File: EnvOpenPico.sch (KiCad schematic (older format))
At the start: 37 parts, among them J2 B3U-1000P, J3 2.54mm header 01x20, J4 2.54mm header 01x20, J5 Conn_01x03_Male, U1 SPX3819M5-L-3-3, U3 RP2040, X1 XO 32 12Mhz 3225 seiko

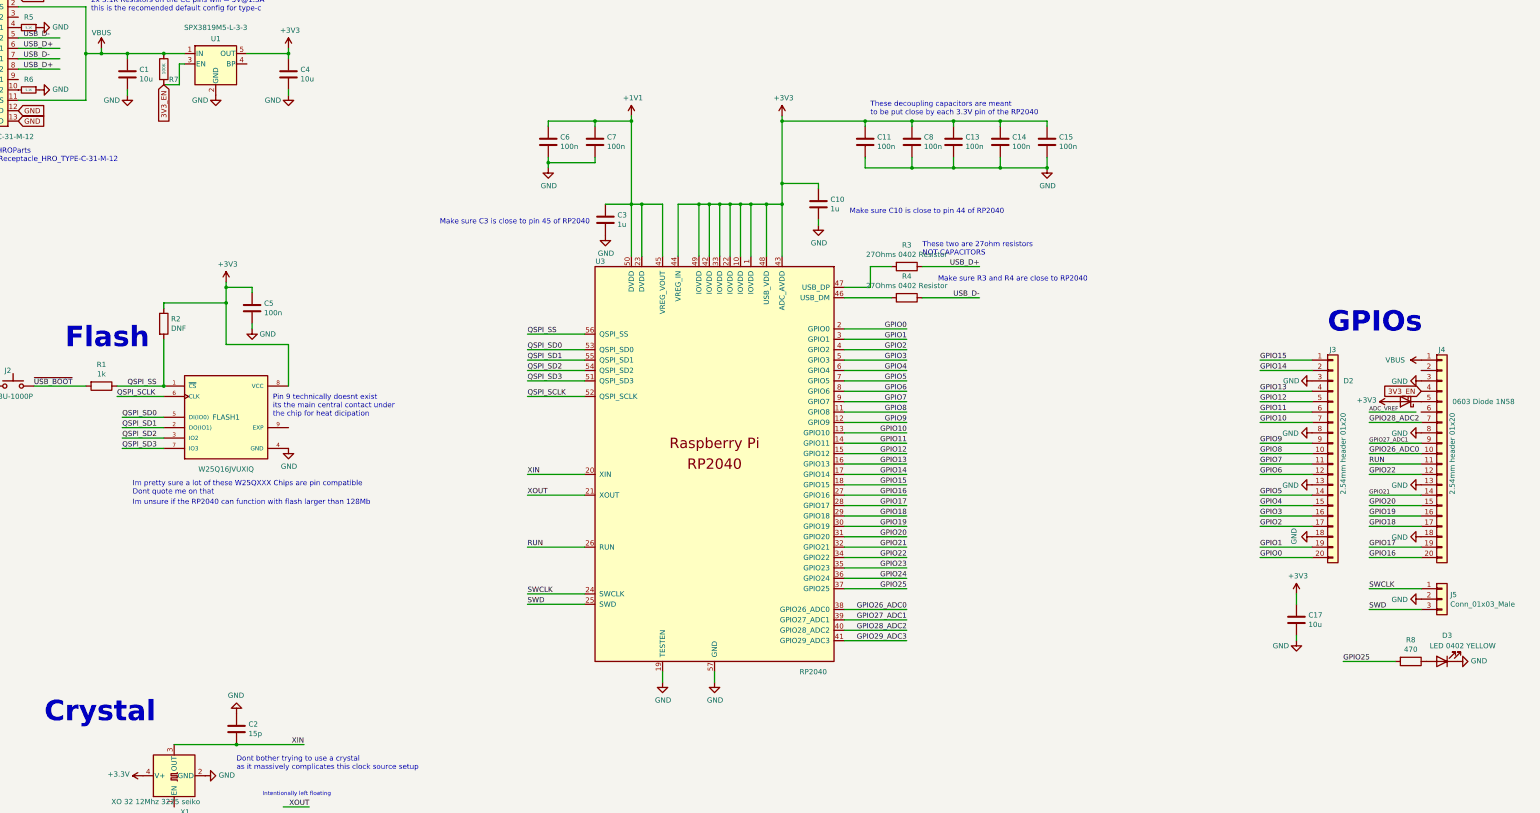
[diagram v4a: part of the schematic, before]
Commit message: Generated updated Gerber files with castelations
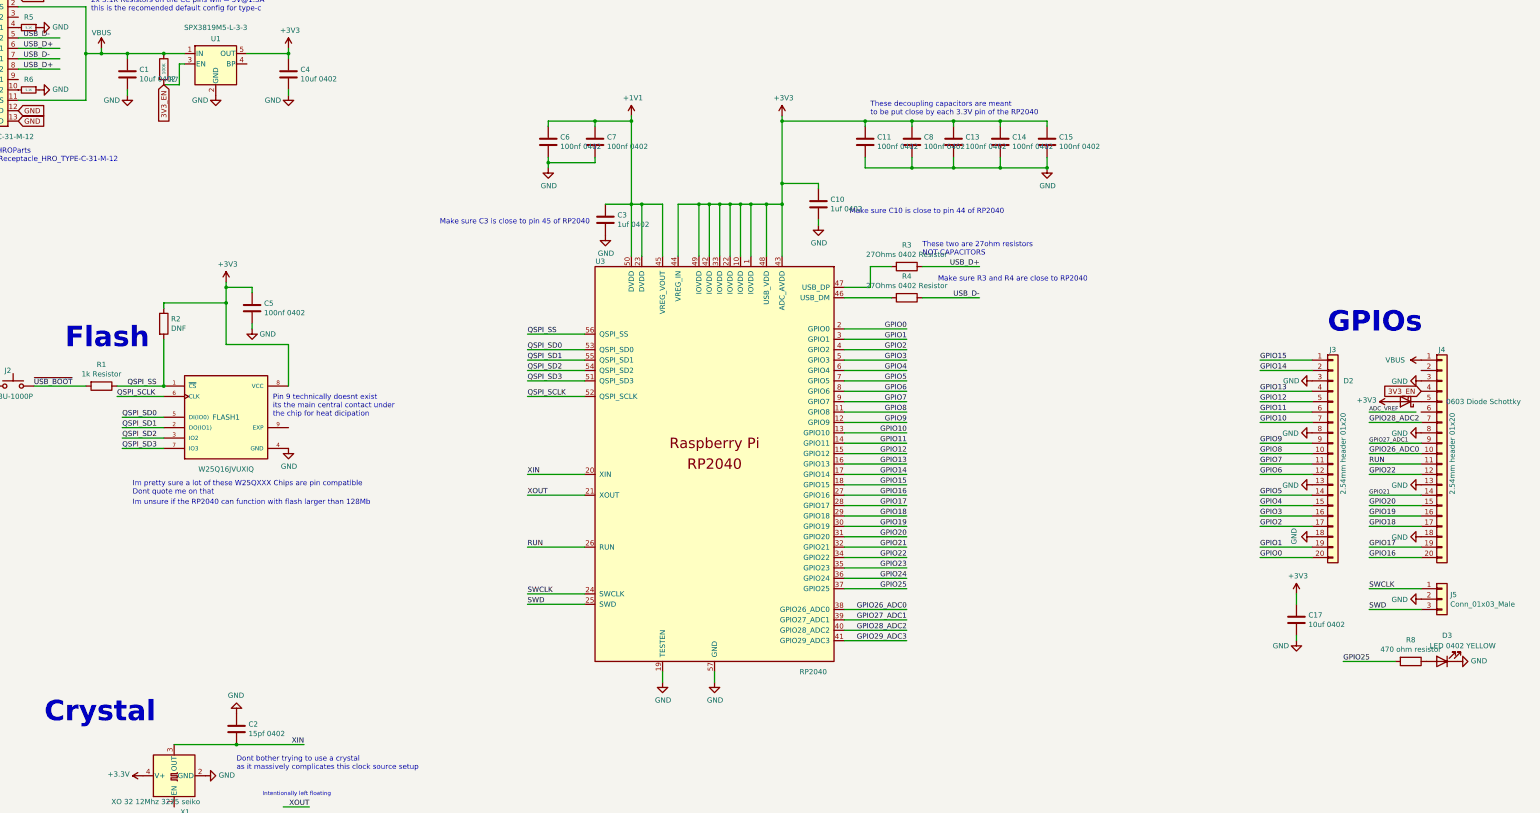
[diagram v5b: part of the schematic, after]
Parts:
- C1, C17, C4: value 10u -> 10uf 0402
- C10, C3: value 1u -> 1uf 0402
- C11, C13, C14, C15, C5, C6, C7, C8: value 100n -> 100nf 0402
- C2: value 15p -> 15pf 0402
- D2: value 0603 Diode 1N58 -> 0603 Diode Schottky
- R1: value 1k -> 1k Resistor
- R8: value 470 -> 470 ohm resistor
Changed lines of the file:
@@
 F 1 "TYPE-C-31-M-12" H 1250 950 50  0000 R CNN
 F 2 "HRO-TYPE-C31-M-12:HRO-TYPE-C-31-M-12" H 1150 1700 50  0001 C CNN
-F 3 "~" H 1150 1700 50  0001 C CNN
+F 3 "" H 1150 1700 50  0001 C CNN
 	1    1000 1750
 	1    0    0    -1
@@
 F 1 " 27Ohms 0402 Resistor" V 9534 4100 50  0000 C CNN
 F 2 "Capacitor_SMD:C_0402_1005Metric" V 9580 4100 50  0001 C CNN
-F 3 "~" H 9650 4100 50  0001 C CNN
+F 3 "" H 9650 4100 50  0001 C CNN
 	1    9650 4100
 	0    1    1    0
@@
 P 6200 2600
 F 0 "C6" H 6315 2646 50  0000 L CNN
-F 1 "100n" H 6315 2555 50  0000 L CNN
+F 1 "100nf 0402" H 6315 2555 50  0000 L CNN
 F 2 "Capacitor_SMD:C_0402_1005Metric" H 6238 2450 50  0001 C CNN
-F 3 "~" H 6200 2600 50  0001 C CNN
+F 3 "" H 6200 2600 50  0001 C CNN
 	1    6200 2600
 	1    0    0    -1
@@
 P 6650 2600
 F 0 "C7" H 6765 2646 50  0000 L CNN
-F 1 "100n" H 6765 2555 50  0000 L CNN
+F 1 "100nf 0402" H 6765 2555 50  0000 L CNN
 F 2 "Capacitor_SMD:C_0402_1005Metric" H 6688 2450 50  0001 C CNN
-F 3 "~" H 6650 2600 50  0001 C CNN
+F 3 "" H 6650 2600 50  0001 C CNN
 	1    6650 2600
 	1    0    0    -1
@@
 P 8800 3200
 F 0 "C10" H 8915 3246 50  0000 L CNN
-F 1 "1u" H 8915 3155 50  0000 L CNN
+F 1 "1uf 0402" H 8915 3155 50  0000 L CNN
 F 2 "Capacitor_SMD:C_0402_1005Metric" H 8838 3050 50  0001 C CNN
-F 3 "~" H 8800 3200 50  0001 C CNN
+F 3 "" H 8800 3200 50  0001 C CNN
 	1    8800 3200
 	1    0    0    -1
@@
 P 3350 4200
 F 0 "C5" H 3465 4246 50  0000 L CNN
-F 1 "100n" H 3465 4155 50  0000 L CNN
+F 1 "100nf 0402" H 3465 4155 50  0000 L CNN
 F 2 "Capacitor_SMD:C_0402_1005Metric" H 3388 4050 50  0001 C CNN
-F 3 "~" H 3350 4200 50  0001 C CNN
+F 3 "" H 3350 4200 50  0001 C CNN
 	1    3350 4200
 	1    0    0    -1
@@
 P 1900 4950
 F 0 "R1" V 1693 4950 50  0000 C CNN
-F 1 "1k" V 1784 4950 50  0000 C CNN
+F 1 "1k Resistor" V 1784 4950 50  0000 C CNN
 F 2 "Capacitor_SMD:C_0402_1005Metric" V 1830 4950 50  0001 C CNN
-F 3 "~" H 1900 4950 50  0001 C CNN
+F 3 "" H 1900 4950 50  0001 C CNN
 	1    1900 4950
 	0    1    1    0
@@
 F 1 "DNF" H 2570 4305 50  0000 L CNN
 F 2 "Capacitor_SMD:C_0402_1005Metric" V 2430 4350 50  0001 C CNN
-F 3 "~" H 2500 4350 50  0001 C CNN
+F 3 "" H 2500 4350 50  0001 C CNN
 	1    2500 4350
 	1    0    0    -1
@@
 F 1 "SPX3819M5-L-3-3" H 3000 2200 50  0000 C CNN
 F 2 "Package_TO_SOT_SMD:SOT-23-5" H 3000 2050 50  0001 C CNN
-F 3 "~" H 3100 1600 50  0001 C CNN
+F 3 "" H 3100 1600 50  0001 C CNN
 	1    3000 1850
 	1    0    0    -1
@@
 P 2150 1950
 F 0 "C1" H 2265 1996 50  0000 L CNN
-F 1 "10u" H 2265 1905 50  0000 L CNN
+F 1 "10uf 0402" H 2265 1905 50  0000 L CNN
 F 2 "Capacitor_SMD:C_0402_1005Metric" H 2188 1800 50  0001 C CNN
-F 3 "~" H 2150 1950 50  0001 C CNN
+F 3 "" H 2150 1950 50  0001 C CNN
 	1    2150 1950
 	1    0    0    -1
@@
 P 3700 1950
 F 0 "C4" H 3815 1996 50  0000 L CNN
-F 1 "10u" H 3815 1905 50  0000 L CNN
+F 1 "10uf 0402" H 3815 1905 50  0000 L CNN
 F 2 "Capacitor_SMD:C_0402_1005Metric" H 3738 1800 50  0001 C CNN
-F 3 "~" H 3700 1950 50  0001 C CNN
+F 3 "" H 3700 1950 50  0001 C CNN
 	1    3700 1950
 	1    0    0    -1
@@
 F 1 "B3U-1000P" H 1050 4850 50  0000 C CNN
 F 2 "Button_Switch_SMD:SW_SPST_B3U-1000P" H 1050 4950 50  0001 C CNN
-F 3 "~" H 1050 4950 50  0001 C CNN
+F 3 "" H 1050 4950 50  0001 C CNN
 	1    1050 4950
 	-1   0    0    -1
@@
 F 1 " 27Ohms  0402 Resistor" V 9534 3800 50  0000 C CNN
 F 2 "Capacitor_SMD:C_0402_1005Metric" V 9580 3800 50  0001 C CNN
-F 3 "~" H 9650 3800 50  0001 C CNN
+F 3 "" H 9650 3800 50  0001 C CNN
 	1    9650 3800
 	0    1    1    0
@@
 F 1 "2.54mm header 01x20" V 14900 5600 50  0000 C CNN
 F 2 "Connector_PinHeader_2.54mm:PinHeader_1x20_P2.54mm_Vertical" H 14800 5600 50  0001 C CNN
-F 3 "~" H 14800 5600 50  0001 C CNN
+F 3 "" H 14800 5600 50  0001 C CNN
 	1    14800 5600
 	1    0    0    -1
@@
 F 1 "2.54mm header 01x20" V 13850 5600 50  0000 C CNN
 F 2 "Connector_PinHeader_2.54mm:PinHeader_1x20_P2.54mm_Vertical" H 13750 5600 50  0001 C CNN
-F 3 "~" H 13750 5600 50  0001 C CNN
+F 3 "" H 13750 5600 50  0001 C CNN
 	1    13750 5600
 	1    0    0    -1
@@
 F 1 "MountingHole" H 10000 10155 50  0000 L CNN
 F 2 "MountingHole:MountingHole_2.2mm_M2" H 9900 10200 50  0001 C CNN
-F 3 "~" H 9900 10200 50  0001 C CNN
+F 3 "" H 9900 10200 50  0001 C CNN
 	1    9900 10200
 	1    0    0    -1
@@
 F 1 "MountingHole" H 10000 10355 50  0000 L CNN
 F 2 "MountingHole:MountingHole_2.2mm_M2" H 9900 10400 50  0001 C CNN
-F 3 "~" H 9900 10400 50  0001 C CNN
+F 3 "" H 9900 10400 50  0001 C CNN
 	1    9900 10400
 	1    0    0    -1
@@
 F 1 "MountingHole" H 10000 10555 50  0000 L CNN
 F 2 "MountingHole:MountingHole_2.2mm_M2" H 9900 10600 50  0001 C CNN
-F 3 "~" H 9900 10600 50  0001 C CNN
+F 3 "" H 9900 10600 50  0001 C CNN
 	1    9900 10600
 	1    0    0    -1
@@
 F 1 "MountingHole" H 10000 10755 50  0000 L CNN
 F 2 "MountingHole:MountingHole_2.2mm_M2" H 9900 10800 50  0001 C CNN
-F 3 "~" H 9900 10800 50  0001 C CNN
+F 3 "" H 9900 10800 50  0001 C CNN
 	1    9900 10800
 	1    0    0    -1
@@
 P 13400 7200
 F 0 "C17" H 13515 7246 50  0000 L CNN
-F 1 "10u" H 13515 7155 50  0000 L CNN
+F 1 "10uf 0402" H 13515 7155 50  0000 L CNN
 F 2 "Capacitor_SMD:C_0402_1005Metric" H 13438 7050 50  0001 C CNN
-F 3 "~" H 13400 7200 50  0001 C CNN
+F 3 "" H 13400 7200 50  0001 C CNN
 	1    13400 7200
 	1    0    0    -1
@@
 P 14450 5100
 F 0 "D2" H 15000 4900 50  0000 C CNN
-F 1 "0603 Diode 1N58" H 13700 5100 50  0000 C CNN
+F 1 "0603 Diode Schottky" H 13700 5100 50  0000 C CNN
 F 2 "Diode_SMD:D_0603_1608Metric" H 14450 5100 50  0001 C CNN
-F 3 "~" H 14450 5100 50  0001 C CNN
+F 3 "" H 14450 5100 50  0001 C CNN
 	1    14450 5100
 	-1   0    0    1
@@
 P 14500 7600
 F 0 "R8" V 14293 7600 50  0000 C CNN
-F 1 "470" V 14384 7600 50  0000 C CNN
+F 1 "470 ohm resistor" V 14384 7600 50  0000 C CNN
 F 2 "Resistor_SMD:R_0402_1005Metric" V 14430 7600 50  0001 C CNN
-F 3 "~" H 14500 7600 50  0001 C CNN
+F 3 "" H 14500 7600 50  0001 C CNN
 	1    14500 7600
 	0    1    1    0
@@
 F 1 "LED 0402 YELLOW" H 14600 7450 50  0000 C CNN
 F 2 "LED_SMD:LED_0402_1005Metric" H 14800 7600 50  0001 C CNN
-F 3 "~" H 14800 7600 50  0001 C CNN
+F 3 "" H 14800 7600 50  0001 C CNN
 	1    14800 7600
 	-1   0    0    1
@@
 F 1 "Conn_01x03_Male" H 14880 6951 50  0000 L CNN
 F 2 "Connector_PinHeader_2.54mm:PinHeader_1x03_P2.54mm_Vertical" H 14800 7000 50  0001 C CNN
-F 3 "~" H 14800 7000 50  0001 C CNN
+F 3 "" H 14800 7000 50  0001 C CNN
 	1    14800 7000
 	1    0    0    -1
@@
 P 9250 2600
 F 0 "C11" H 9365 2646 50  0000 L CNN
-F 1 "100n" H 9365 2555 50  0000 L CNN
+F 1 "100nf 0402" H 9365 2555 50  0000 L CNN
 F 2 "Capacitor_SMD:C_0402_1005Metric" H 9288 2450 50  0001 C CNN
-F 3 "~" H 9250 2600 50  0001 C CNN
+F 3 "" H 9250 2600 50  0001 C CNN
 	1    9250 2600
 	1    0    0    -1
@@
 P 11000 2600
 F 0 "C15" H 11115 2646 50  0000 L CNN
-F 1 "100n" H 11115 2555 50  0000 L CNN
+F 1 "100nf 0402" H 11115 2555 50  0000 L CNN
 F 2 "Capacitor_SMD:C_0402_1005Metric" H 11038 2450 50  0001 C CNN
-F 3 "~" H 11000 2600 50  0001 C CNN
+F 3 "" H 11000 2600 50  0001 C CNN
 	1    11000 2600
 	1    0    0    -1
@@
 P 10550 2600
 F 0 "C14" H 10665 2646 50  0000 L CNN
-F 1 "100n" H 10665 2555 50  0000 L CNN
+F 1 "100nf 0402" H 10665 2555 50  0000 L CNN
 F 2 "Capacitor_SMD:C_0402_1005Metric" H 10588 2450 50  0001 C CNN
-F 3 "~" H 10550 2600 50  0001 C CNN
+F 3 "" H 10550 2600 50  0001 C CNN
 	1    10550 2600
 	1    0    0    -1
@@
 P 10100 2600
 F 0 "C13" H 10215 2646 50  0000 L CNN
-F 1 "100n" H 10215 2555 50  0000 L CNN
+F 1 "100nf 0402" H 10215 2555 50  0000 L CNN
 F 2 "Capacitor_SMD:C_0402_1005Metric" H 10138 2450 50  0001 C CNN
-F 3 "~" H 10100 2600 50  0001 C CNN
+F 3 "" H 10100 2600 50  0001 C CNN
 	1    10100 2600
 	1    0    0    -1
@@
 F 1 "XO 32 12Mhz 3225 seiko" V 2350 8450 50  0000 L CNN
 F 2 "Crystal:Crystal_SMD_SeikoEpson_TSX3225-4Pin_3.2x2.5mm" H 3300 8350 50  0001 C CNN
-F 3 "http://cdn-reichelt.de/documents/datenblatt/B400/XO32.pdf" H 2500 8700 50  0001 C CNN
+F 3 "" H 2500 8700 50  0001 C CNN
 	1    2600 8700
 	0    -1   -1   0
@@
 P 3200 8250
 F 0 "C2" H 3315 8296 50  0000 L CNN
-F 1 "15p" H 3315 8205 50  0000 L CNN
+F 1 "15pf 0402" H 3315 8205 50  0000 L CNN
 F 2 "Capacitor_SMD:C_0402_1005Metric" H 3238 8100 50  0001 C CNN
-F 3 "~" H 3200 8250 50  0001 C CNN
+F 3 "" H 3200 8250 50  0001 C CNN
 	1    3200 8250
 	1    0    0    -1
@@
 P 6750 3350
 F 0 "C3" H 6865 3396 50  0000 L CNN
-F 1 "1u" H 6865 3305 50  0000 L CNN
+F 1 "1uf 0402" H 6865 3305 50  0000 L CNN
 F 2 "Capacitor_SMD:C_0402_1005Metric" H 6788 3200 50  0001 C CNN
-F 3 "~" H 6750 3350 50  0001 C CNN
+F 3 "" H 6750 3350 50  0001 C CNN
 	1    6750 3350
 	1    0    0    -1
@@
 P 9700 2600
 F 0 "C8" H 9815 2646 50  0000 L CNN
-F 1 "100n" H 9815 2555 50  0000 L CNN
+F 1 "100nf 0402" H 9815 2555 50  0000 L CNN
 F 2 "Capacitor_SMD:C_0402_1005Metric" H 9738 2450 50  0001 C CNN
-F 3 "~" H 9700 2600 50  0001 C CNN
+F 3 "" H 9700 2600 50  0001 C CNN
 	1    9700 2600
 	1    0    0    -1
@@
 F 1 "5.1K" V 1200 2100 20  0000 C CNN
 F 2 "Resistor_SMD:R_0402_1005Metric" H 1200 2100 50  0001 C CNN
-F 3 "~" H 1200 2100 50  0001 C CNN
+F 3 "" H 1200 2100 50  0001 C CNN
 	1    1200 2100
 	0    1    1    0
@@
 F 1 "5.1K" V 1200 1500 20  0000 C CNN
 F 2 "Resistor_SMD:R_0402_1005Metric" H 1200 1500 50  0001 C CNN
-F 3 "~" H 1200 1500 50  0001 C CNN
+F 3 "" H 1200 1500 50  0001 C CNN
 	1    1200 1500
 	0    1    1    0
@@
 F 1 "100K" V 2500 1850 30  0000 L CNN
 F 2 "Resistor_SMD:R_0402_1005Metric" V 2430 1900 50  0001 C CNN
-F 3 "~" H 2500 1900 50  0001 C CNN
+F 3 "" H 2500 1900 50  0001 C CNN
 	1    2500 1900
 	1    0    0    -1

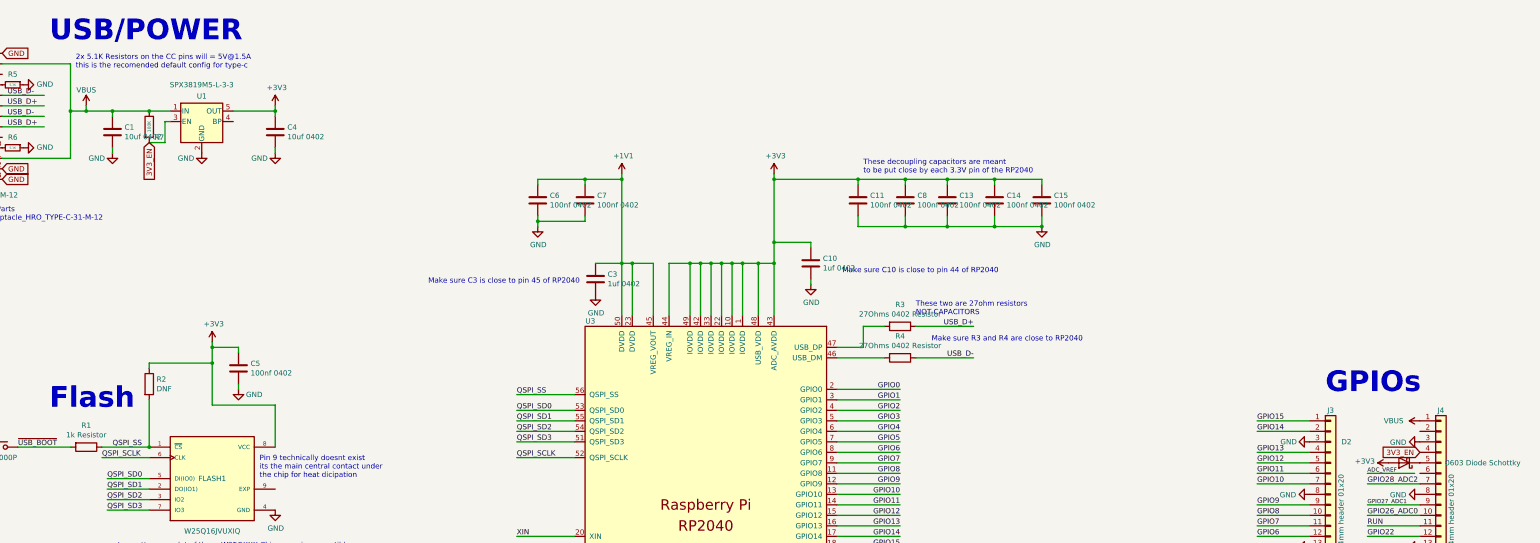
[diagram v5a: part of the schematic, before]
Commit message: unsure if permanent but can get a hold of components RPI Pico uses
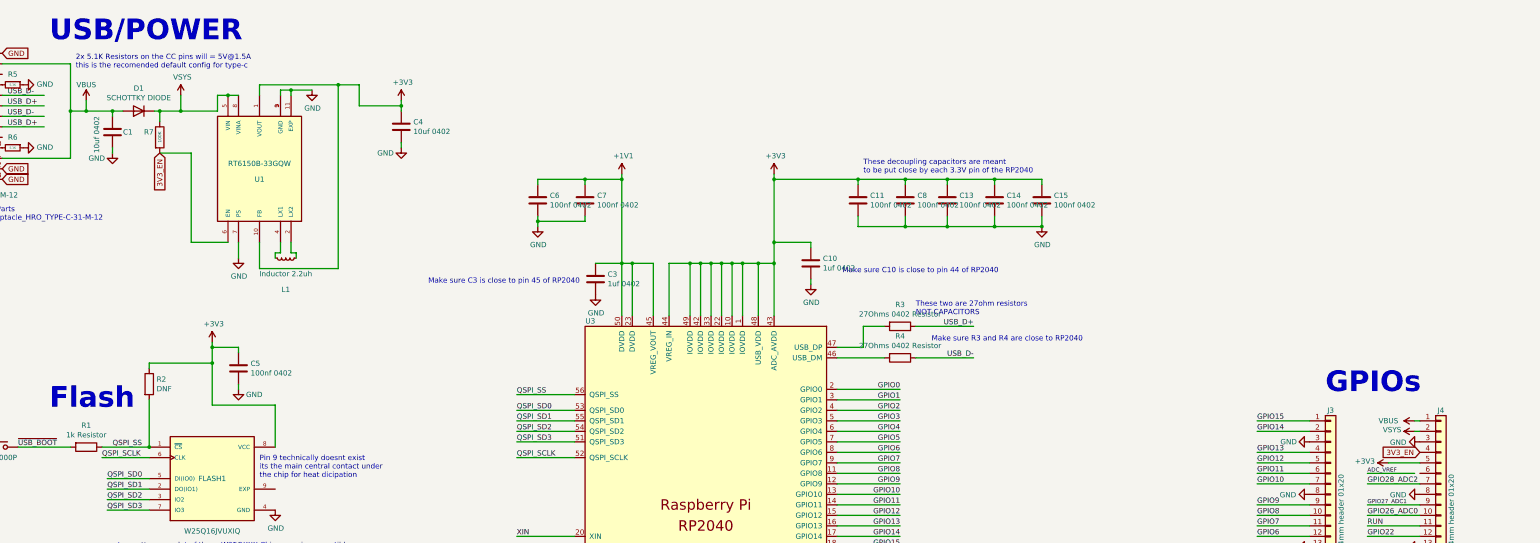
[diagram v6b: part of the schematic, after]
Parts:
- removed D2: 0603 Diode Schottky, Diode_SMD:D_0603_1608Metric, symbol Device:D_Schottky
- removed U1: SPX3819M5-L-3-3, Package_TO_SOT_SMD:SOT-23-5, symbol Regulator_Linear:SPX3819M5-L-3-3
- added D1: SCHOTTKY DIODE, Diode_SMD:D_0603_1608Metric, symbol Simulation_SPICE:DIODE
- added L1: Inductor 2.2uh, Inductor_SMD:L_0805_2012Metric, symbol Device:L_Small
- added U1: RT6150B-33GQW, RT6150B-33GQW:SON50P250X250X80-11N, symbol RT6150B-33GQW:RT6150B-33GQW
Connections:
- net labels added: VSYS
- wire segments 185 -> 213
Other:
- moved on the sheet: C4, R7

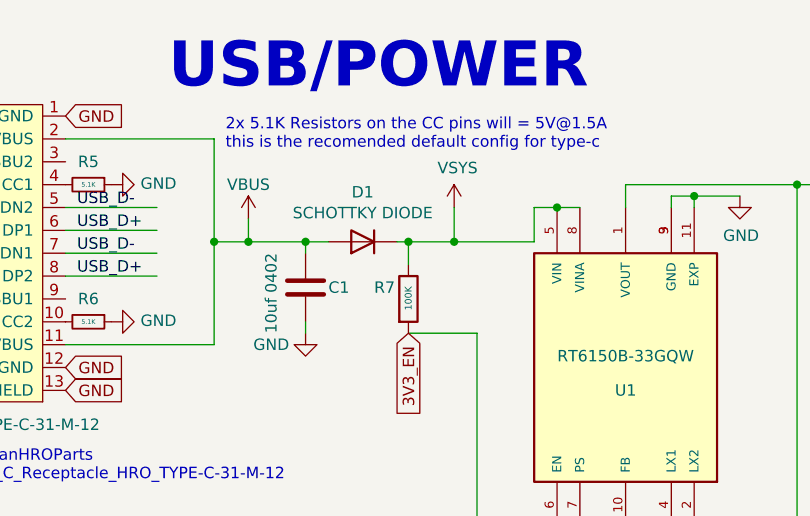
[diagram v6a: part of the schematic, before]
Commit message: Added some vias and tweaked some placements and adjustments
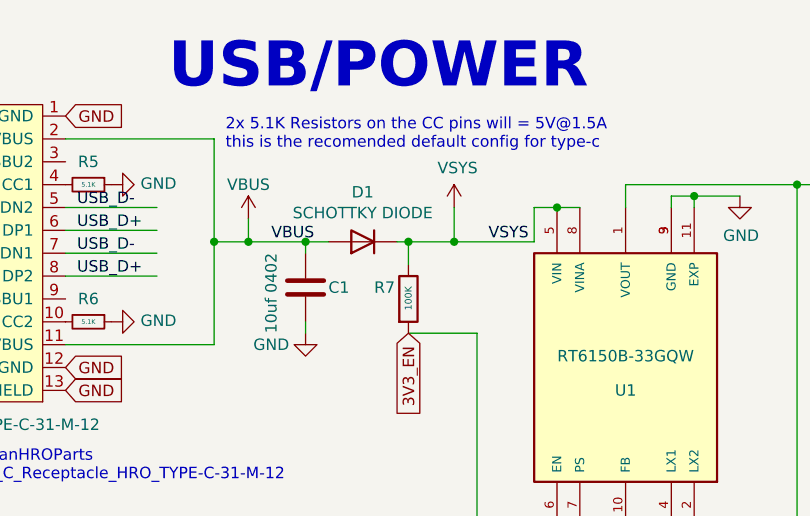
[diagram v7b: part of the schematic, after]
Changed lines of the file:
@@
 Wire Wire Line
 	14300 5100 14600 5100
+Text Label 2950 1750 0    50   ~ 0
+VSYS
+Text Label 2000 1750 0    50   ~ 0
+VBUS
 $EndSCHEMATC
